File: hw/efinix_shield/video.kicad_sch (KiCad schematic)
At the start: 20 parts, among them J2001 VGA, J2002 HDMI_A, U2001 TFP410PAP

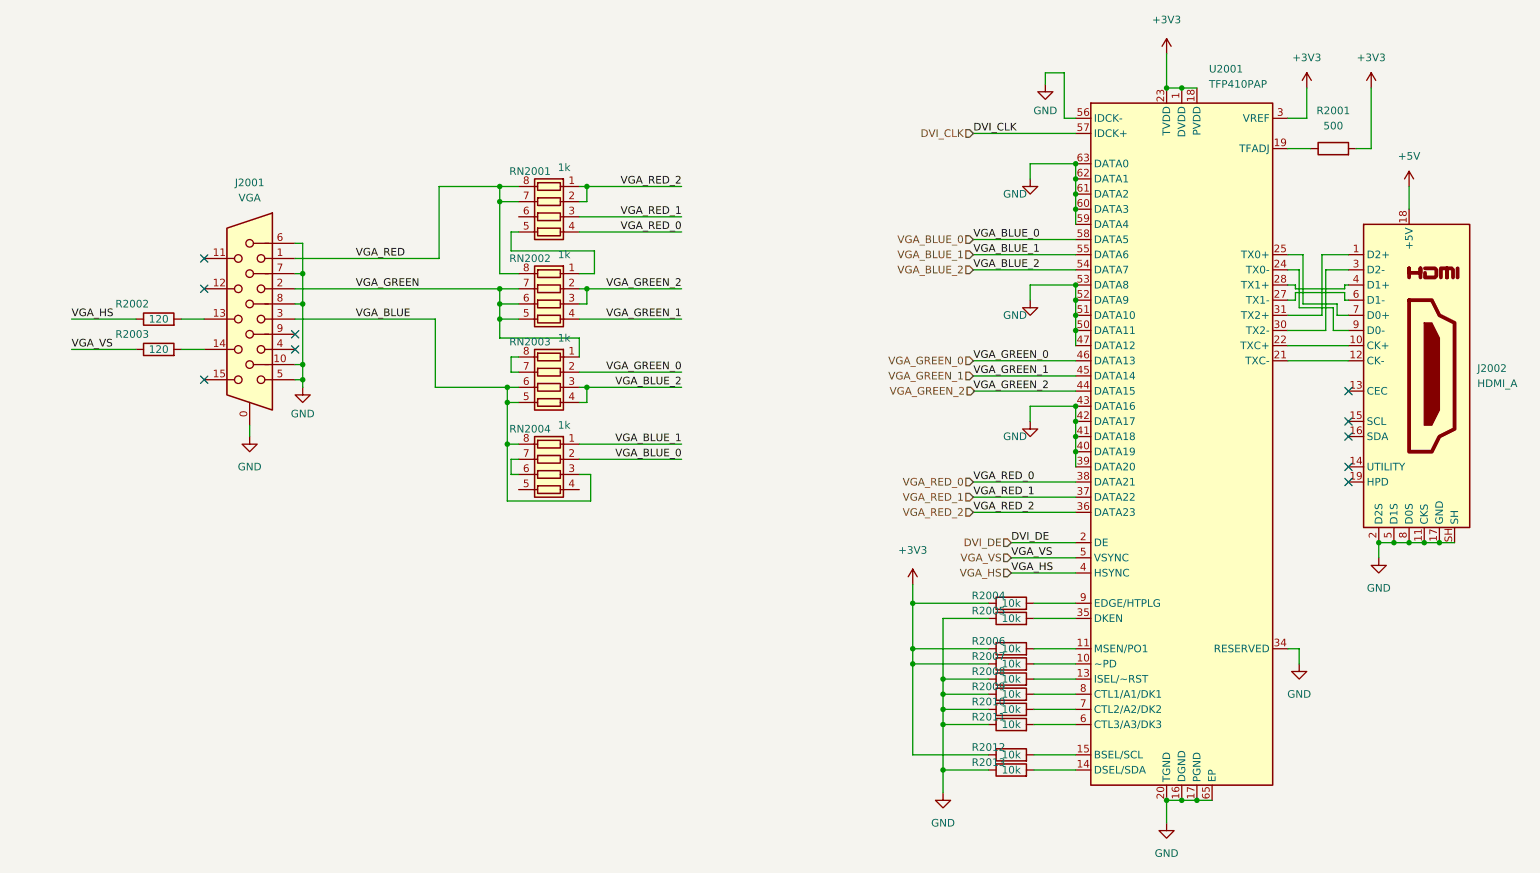
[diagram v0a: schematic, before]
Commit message: Start work on simpler board
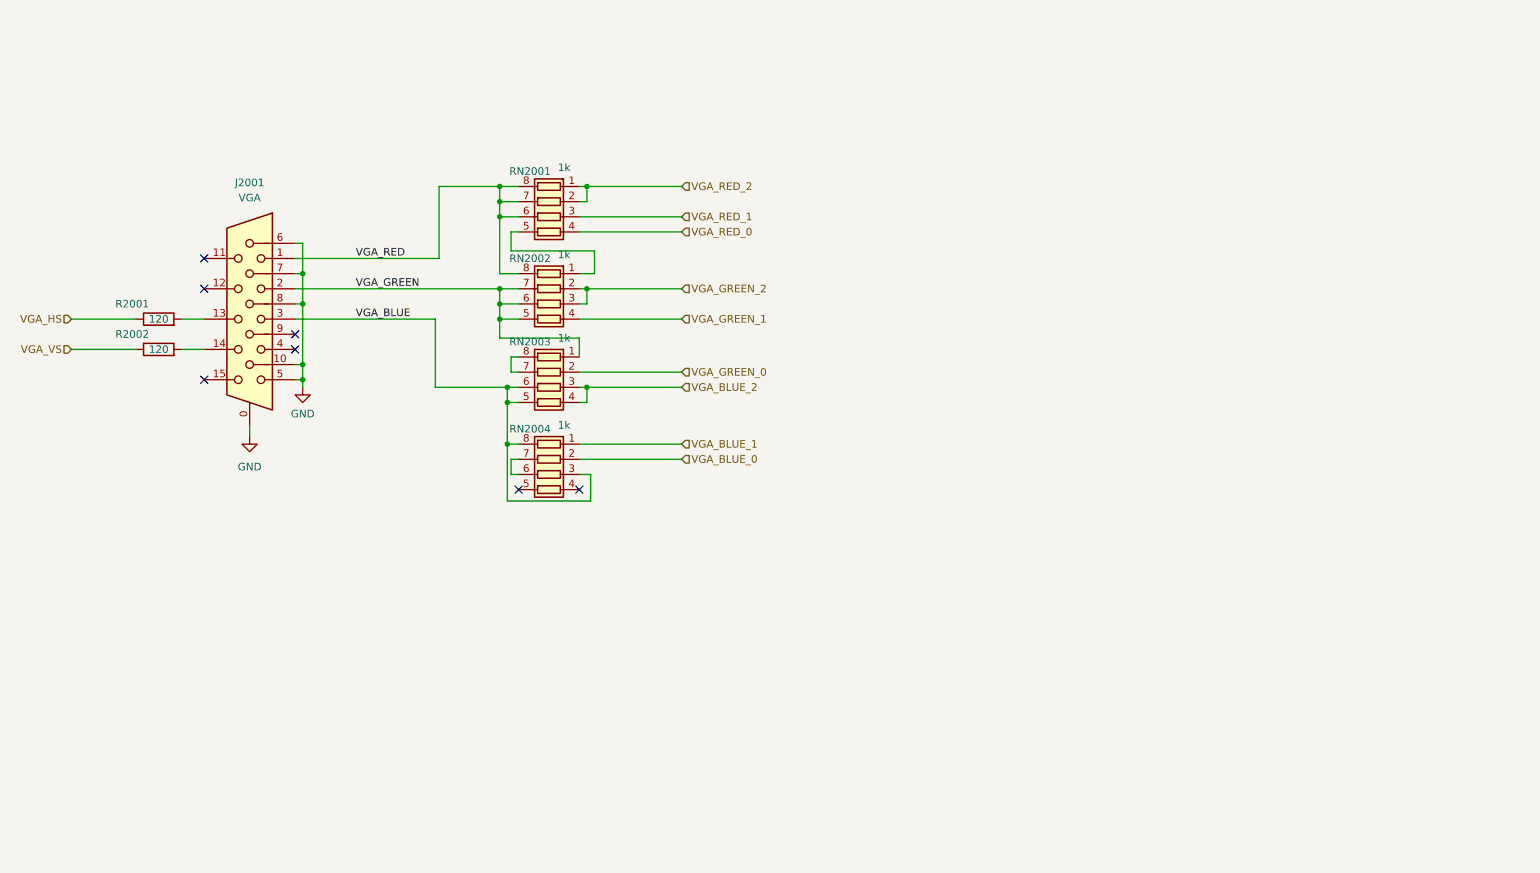
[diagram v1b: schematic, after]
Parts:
- removed J2002: HDMI_A, Connector_HDMI:10029449-111RLF, symbol Connector:HDMI_A
- removed R2001: 500, Resistor_SMD:R_0603_1608Metric_Pad0.98x0.95mm_HandSolder, symbol Device:R
- removed R2004, R2005, R2006, R2007, R2008, R2009, R2010, R2011, R2012, R2013: 10k, Resistor_SMD:R_0603_1608Metric_Pad0.98x0.95mm_HandSolder, symbol Device:R
- removed U2001: TFP410PAP, Package_QFP:HTQFP-64-1EP_10x10mm_P0.5mm_EP8x8mm_Mask4.4x4.4mm_ThermalVias, symbol Video:TFP410PAP
- R2001: renamed from R2002; footprint Resistor_SMD:R_0603_1608Metric_Pad0.98x0.95mm_HandSolder -> Resistor_SMD:R_0805_2012Metric_Pad1.20x1.40mm_HandSolder
- R2002: renamed from R2003; footprint Resistor_SMD:R_0603_1608Metric_Pad0.98x0.95mm_HandSolder -> Resistor_SMD:R_0805_2012Metric_Pad1.20x1.40mm_HandSolder
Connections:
- net VGA_RED: now also RN2001.6 (R3.2)
- no-connect marks 10 -> 7
